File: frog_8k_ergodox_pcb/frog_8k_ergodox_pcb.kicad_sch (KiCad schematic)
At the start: 201 parts, among them J1 USB_C_Receptacle_USB2.0_14P, J2 Conn_01x04_Pin, SW1 SW_DPST_x2, SW2 SW_DPST_x2, U1 PMW3360DM-T2QU, U2 STM32F072CBTx, U3 TLV74318PDBVR, U4 XC6206PxxxMR

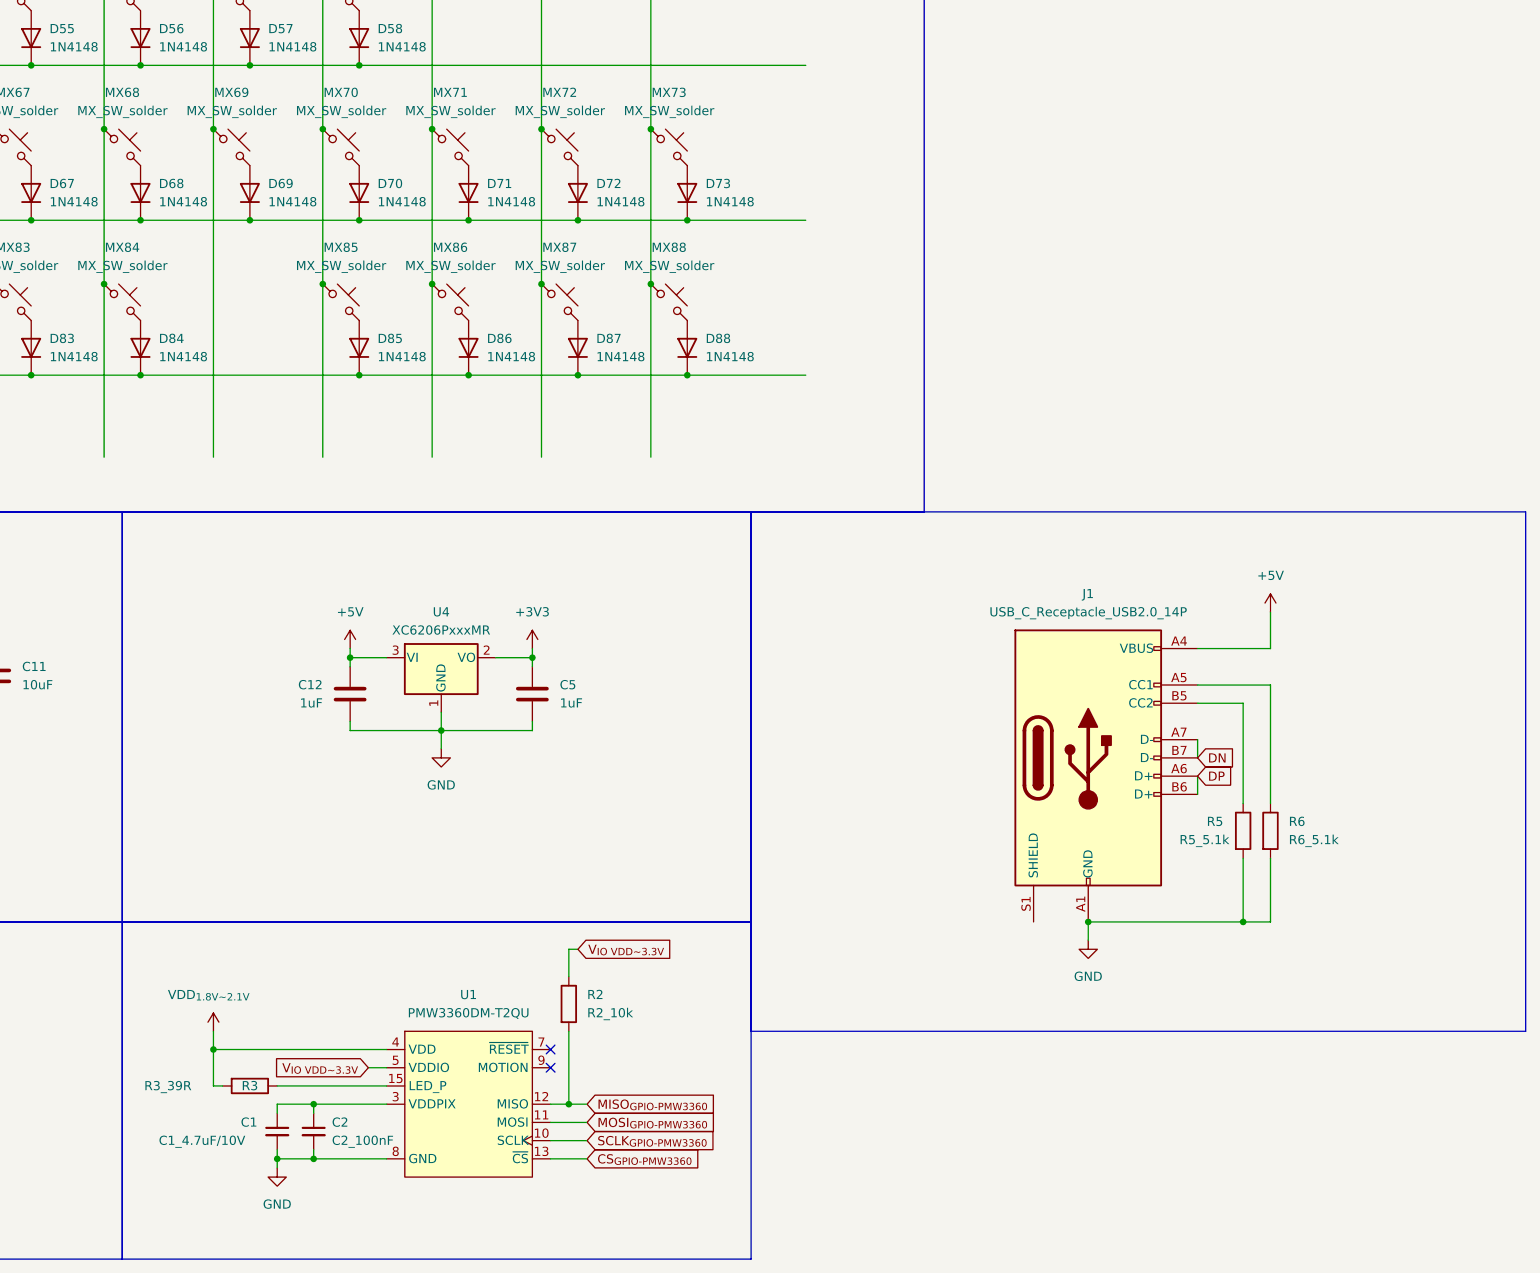
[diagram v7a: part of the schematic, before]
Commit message: Added Pull Up Resistor Symbol on PMW3360 NRESET Pin, Added ESD Protection.
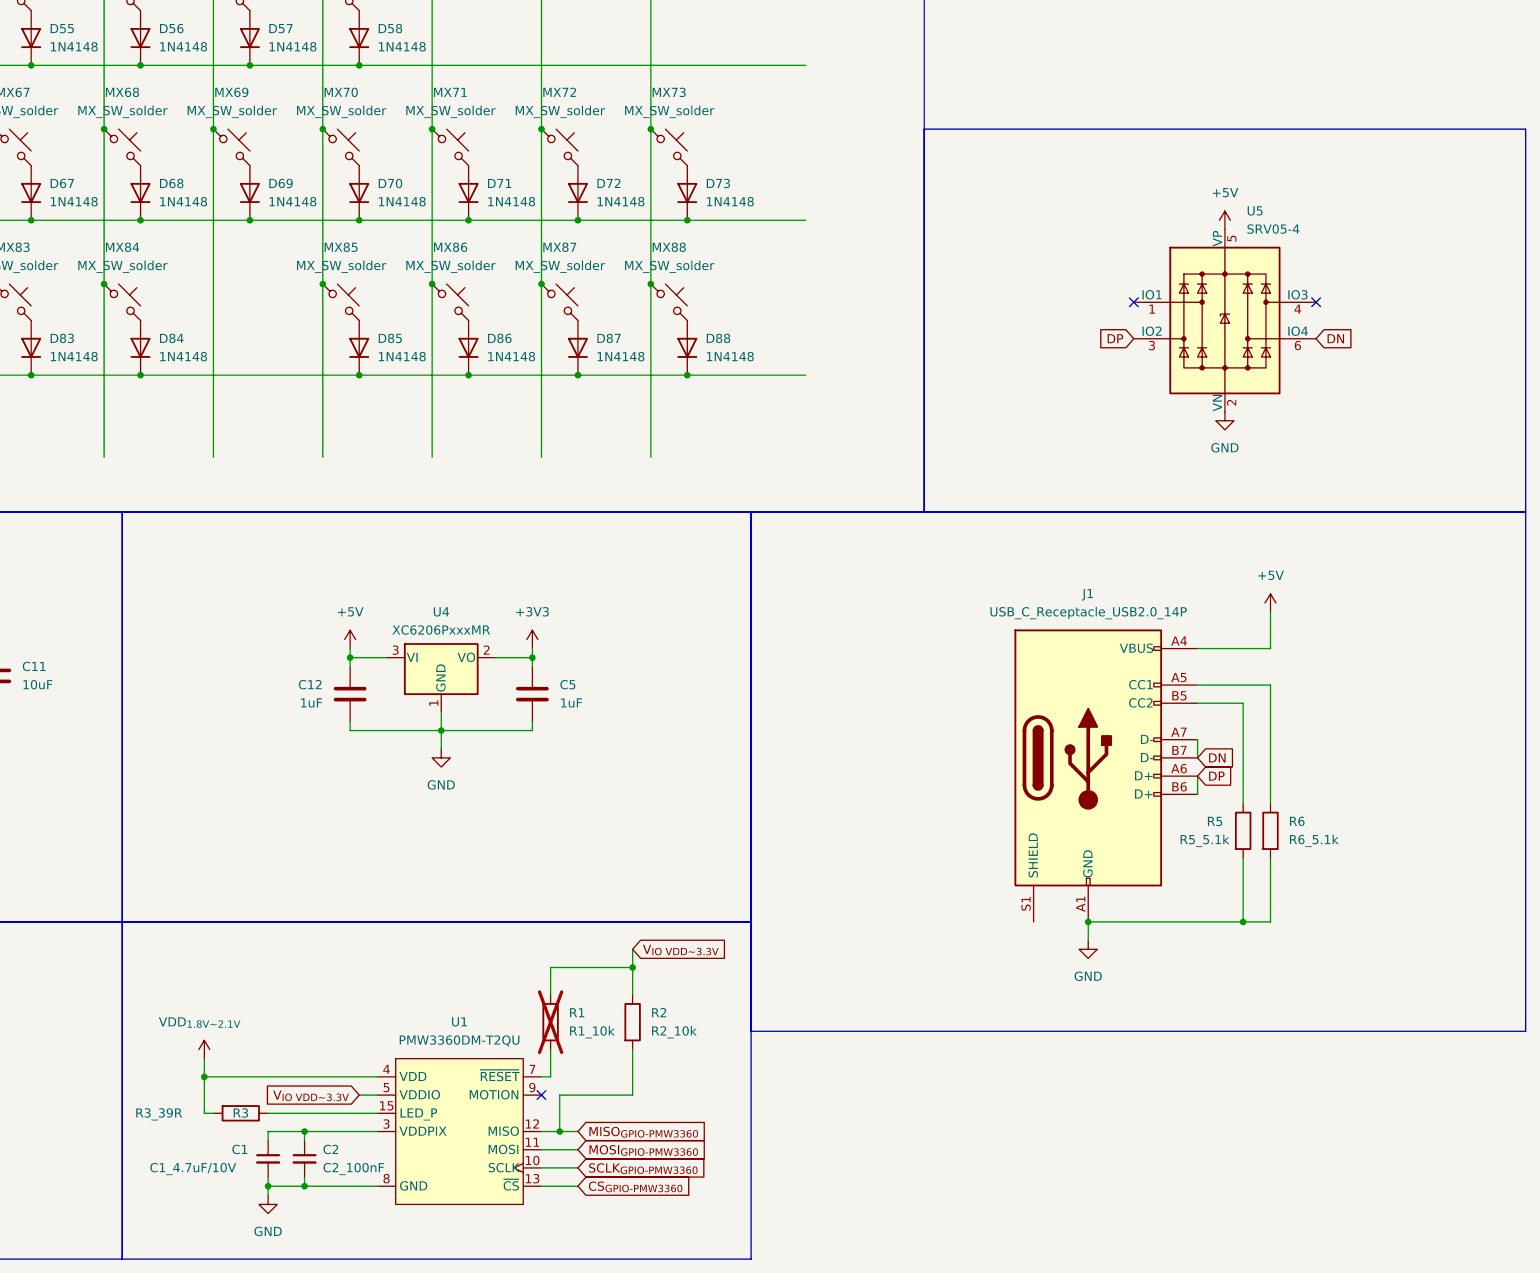
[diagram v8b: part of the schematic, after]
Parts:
- added R1: R1_10k, Resistor_SMD:R_0805_2012Metric_Pad1.20x1.40mm_HandSolder, symbol Device:R
- added U5: SRV05-4, Package_TO_SOT_SMD:SOT-23-6, symbol Power_Protection:SRV05-4
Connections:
- net +5V: now also U5.5 (VP)
- net DN: now also U5.6 (IO4)
- net DP: now also U5.3 (IO2)
- net GND: now also U5.2 (VN)
- net V_{IO VDD~3.3V}: now also R1.1
- net at U1.7 (~{RESET}): now also R1.2
- no-connect marks 3 -> 4
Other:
- moved on the sheet: C1, C2, R2, R3, U1
